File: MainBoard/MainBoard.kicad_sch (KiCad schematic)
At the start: 33 parts, among them J1 1761681-3, J2 Non-Inverting Input, J3 Inverting Input, J4 Output, J5 InvertedOutput, J6 Inverting Input, J7 Non-Inverting Input, J8 Output, J9 InvertedOutput, Q16 BC557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

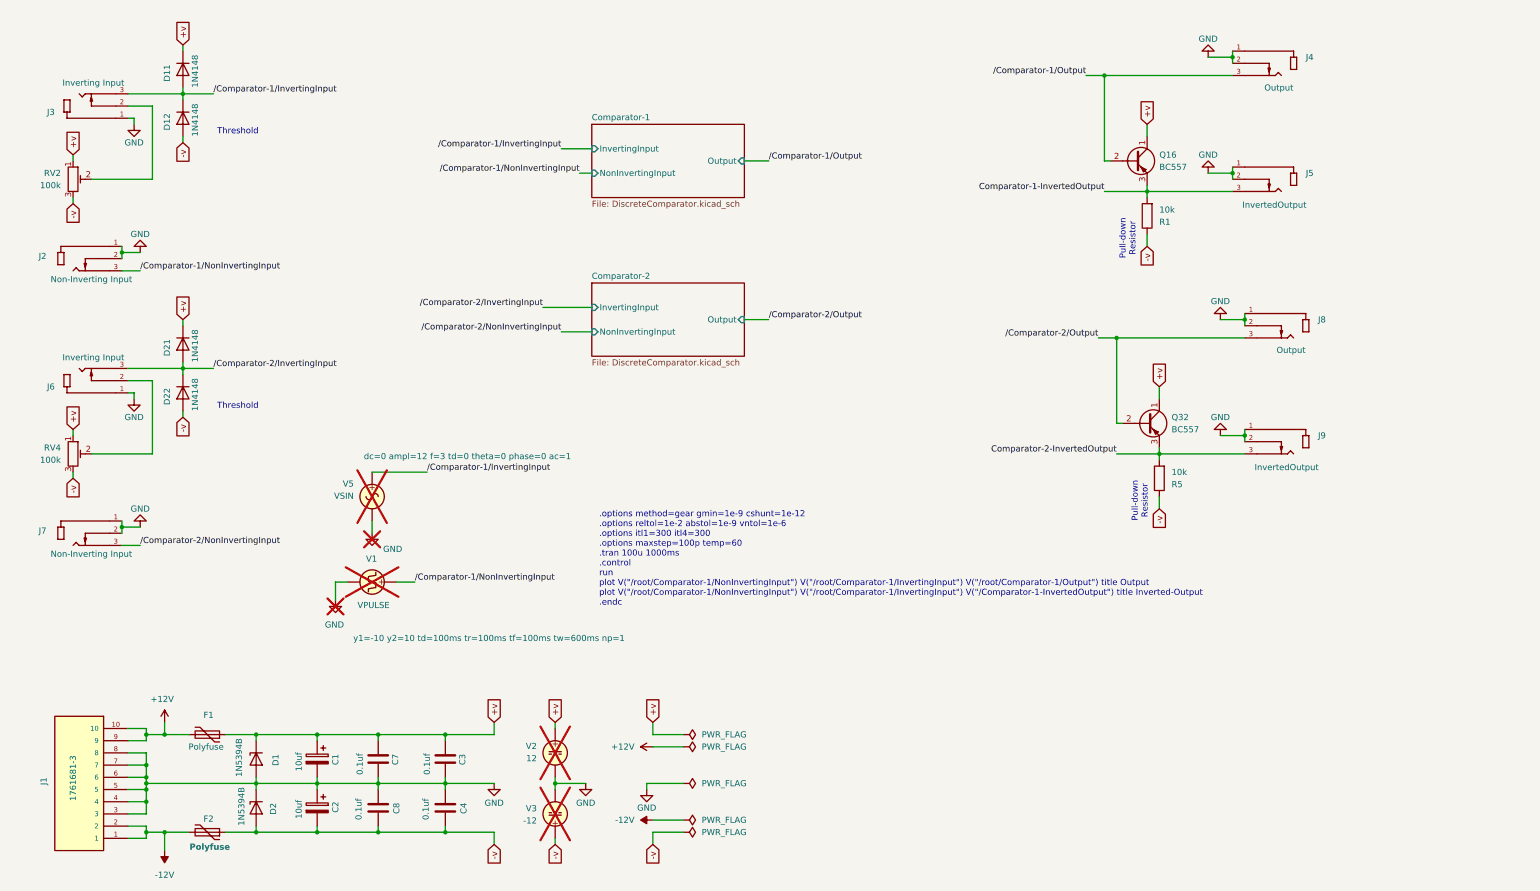
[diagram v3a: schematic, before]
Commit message: updated to be a dual comparator and/or window comparator
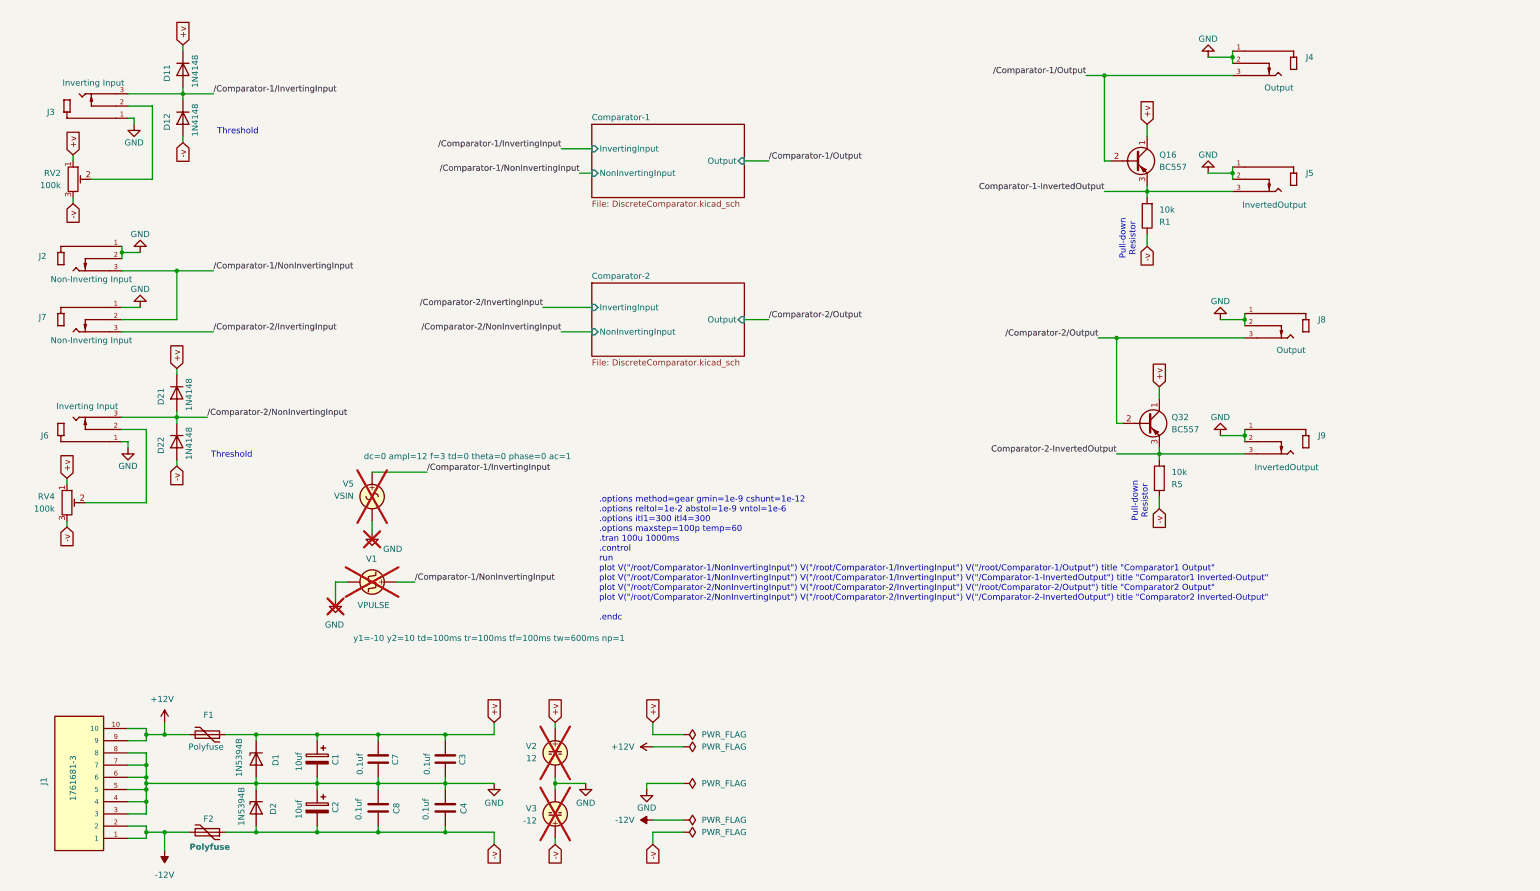
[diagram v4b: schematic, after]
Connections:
- net GND: no longer J7.2
- net /Comparator-1/NonInvertingInput: now also J7.2
- net /Comparator-2/InvertingInput: now also J7.3; no longer D21.2 (A), D22.1 (K), J6.3
- net /Comparator-2/NonInvertingInput: now also D21.2 (A), D22.1 (K), J6.3; no longer J7.3
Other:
- note added: ".options method=gear gmin=1e-9 cshunt=1e-12 .options reltol=1e-2 abstol=1e-9 vntol=1e-6 .options itl1=300 itl4=300 .options maxstep=100p temp=60 .tran 100u 1000ms .control run plot V("/root/Comparator-1/NonInvertingInput") V("/root/Comparator-1/InvertingInput") V("/root/Comparator-1/Output") title "Comparator1 Output" plot V("/root/Comparator-1/NonInvertingInput") V("/root/Comparator-1/InvertingI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"
- note removed: ".options method=gear gmin=1e-9 cshunt=1e-12 .options reltol=1e-2 abstol=1e-9 vntol=1e-6 .options itl1=300 itl4=300 .options maxstep=100p temp=60 .tran 100u 1000ms .control run plot V("/root/Comparator-1/NonInvertingInput") V("/root/Comparator-1/InvertingInput") V("/root/Comparator-1/Output") title Output plot V("/root/Comparator-1/NonInvertingInput") V("/root/Comparator-1/InvertingInput") V("/Com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"
- moved on the sheet: D21, D22, J6, J7, RV4

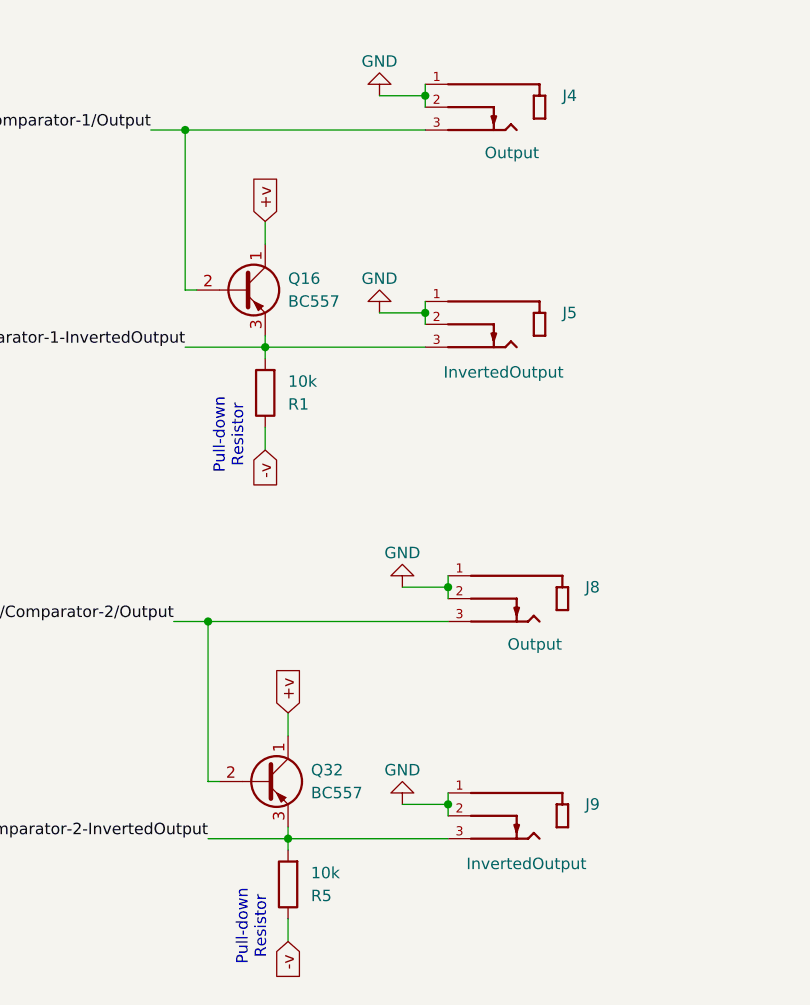
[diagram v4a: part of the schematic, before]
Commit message: fixed output connectors. probably should have ability in model to default them to open when running the simmulation (and keep the ring tied to ground. But , for now tying the ring to tip.
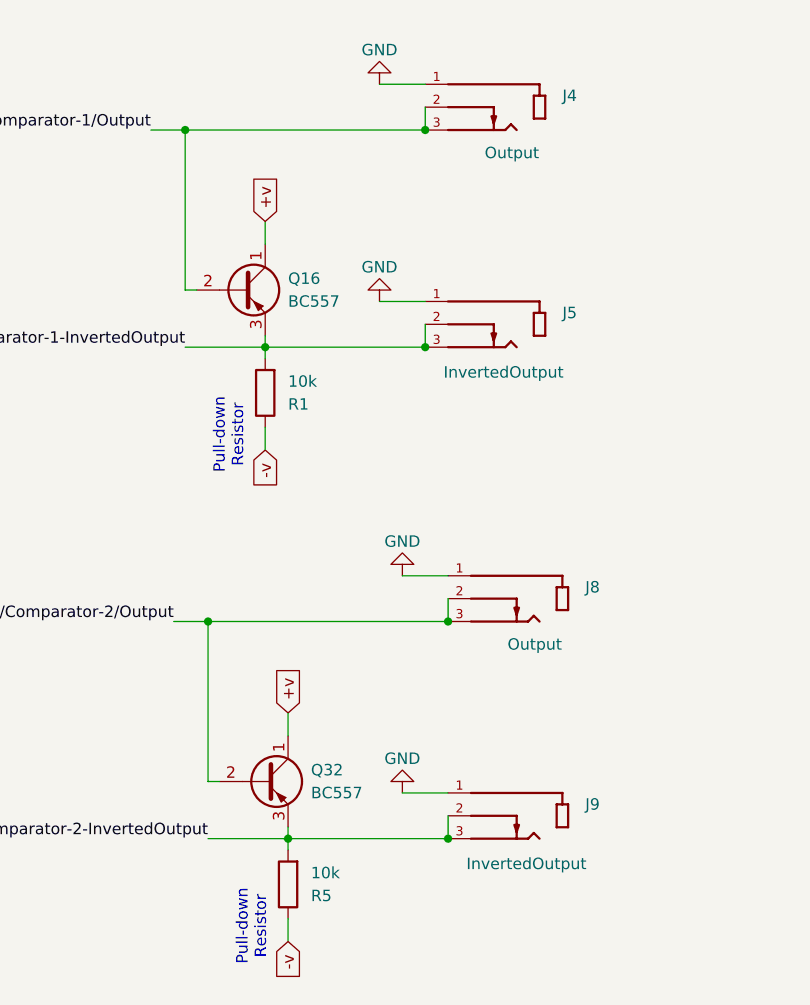
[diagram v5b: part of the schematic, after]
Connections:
- net Comparator-1-InvertedOutput: now also J5.2
- net Comparator-2-InvertedOutput: now also J9.2
- net GND: no longer J4.2, J5.2, J8.2, J9.2
- net /Comparator-1/Output: now also J4.2
- net /Comparator-2/Output: now also J8.2

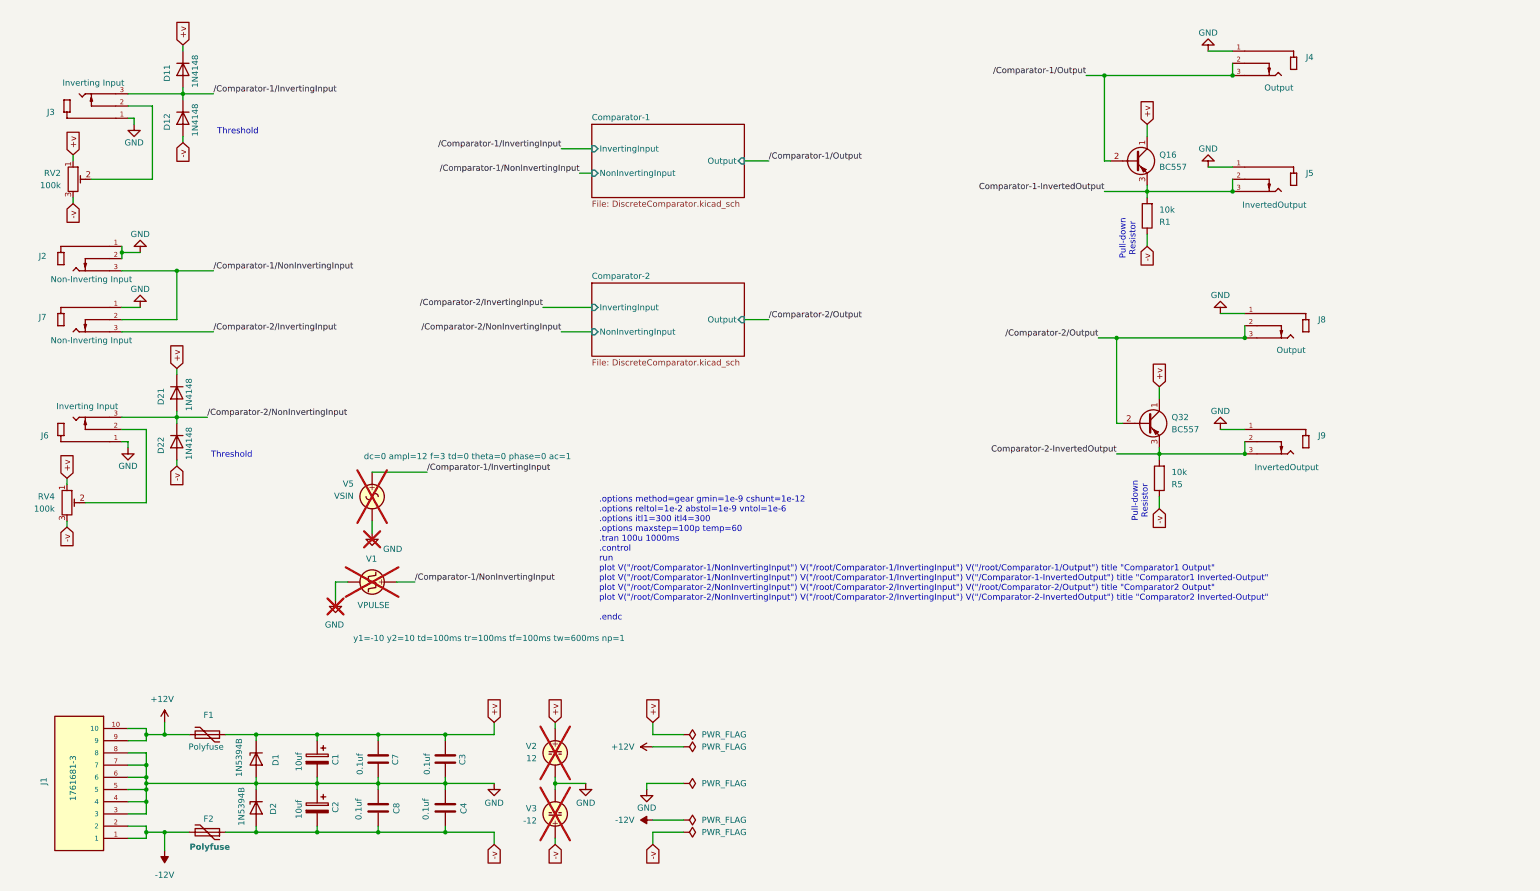
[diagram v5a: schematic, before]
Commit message: functional window comparator
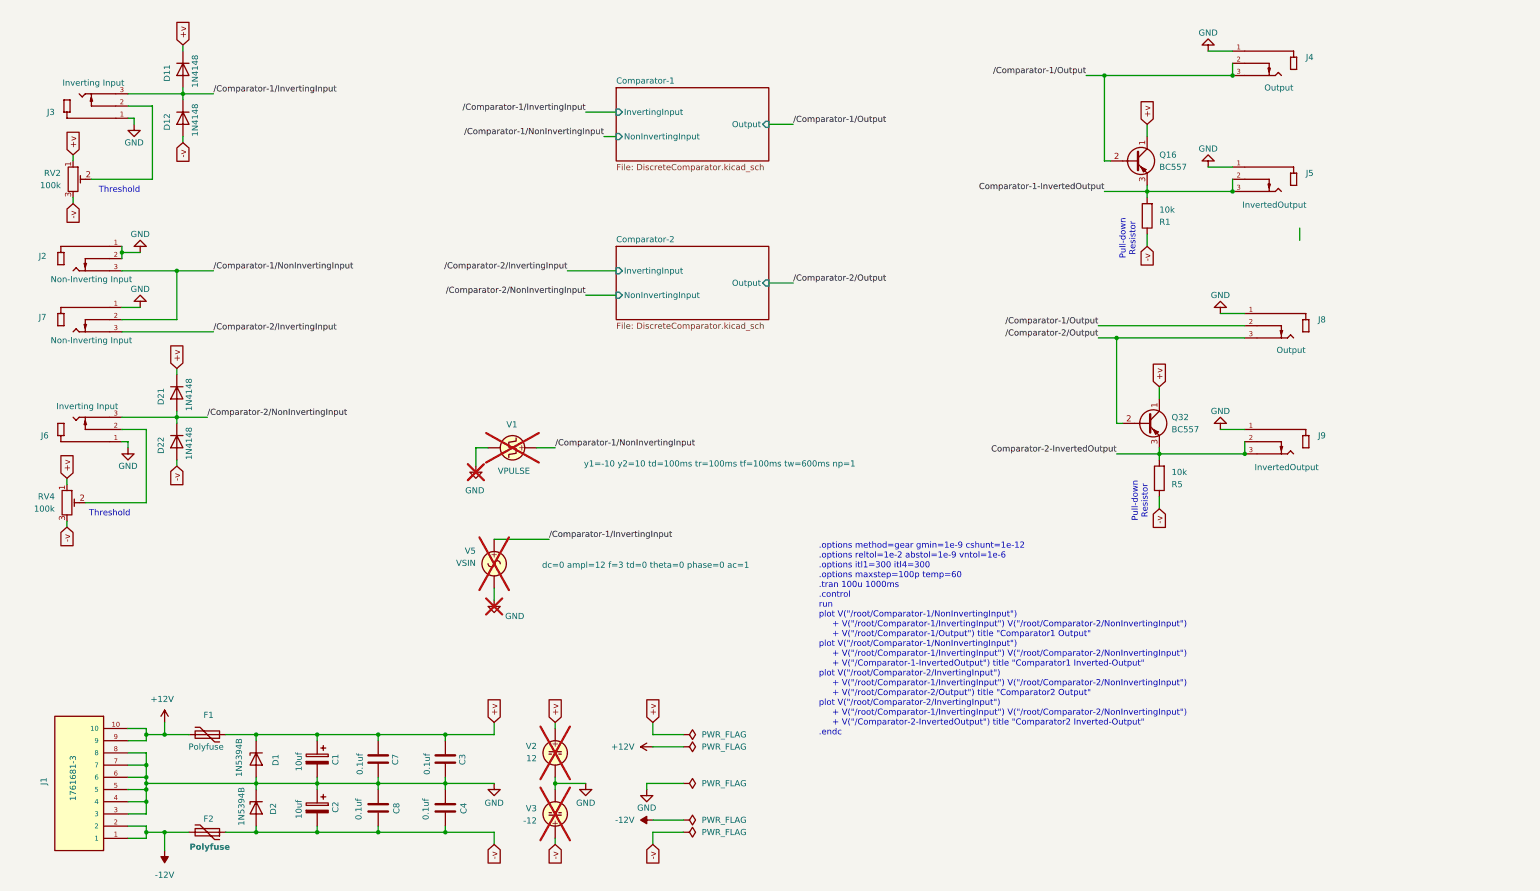
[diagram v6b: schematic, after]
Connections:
- net /Comparator-1/Output: now also J8.2
- net /Comparator-2/Output: no longer J8.2
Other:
- note added: ".options method=gear gmin=1e-9 cshunt=1e-12 .options reltol=1e-2 abstol=1e-9 vntol=1e-6 .options itl1=300 itl4=300 .options maxstep=100p temp=60 .tran 100u 1000ms .control run plot V("/root/Comparator-1/NonInvertingInput") + V("/root/Comparator-1/InvertingInput") V("/root/Comparator-2/NonInvertingInput") + V("/root/Comparator-1/Output") title "Comparator1 Output" plot V("/root/Comparator-1/NonInv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"
- note removed: ".options method=gear gmin=1e-9 cshunt=1e-12 .options reltol=1e-2 abstol=1e-9 vntol=1e-6 .options itl1=300 itl4=300 .options maxstep=100p temp=60 .tran 100u 1000ms .control run plot V("/root/Comparator-1/NonInvertingInput") V("/root/Comparator-1/InvertingInput") V("/root/Comparator-1/Output") title "Comparator1 Output" plot V("/root/Comparator-1/NonInvertingInput") V("/root/Comparator-1/InvertingI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"
- moved on the sheet: V1, V5

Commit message: added over-voltage protection on all inputs and outputs
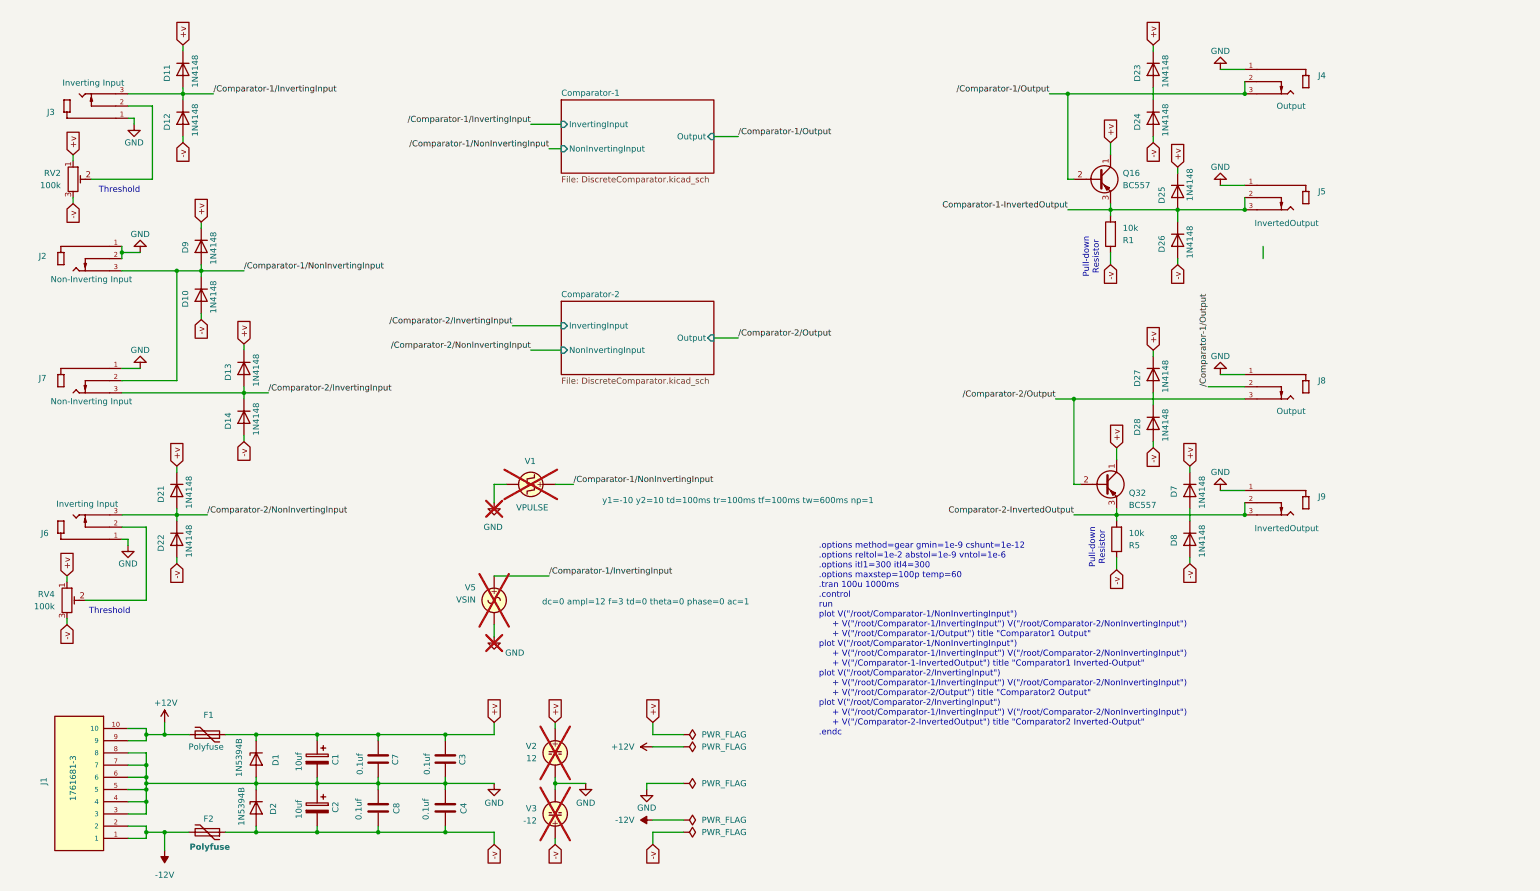
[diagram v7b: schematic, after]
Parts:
- added D10, D13, D14, D23, D24, D25, D26, D27, D28, D7, D8, D9: 1N4148, Diode_THT:D_DO-35_SOD27_P7.62mm_Horizontal, symbol Device:D
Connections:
- net +v: now also D13.1 (K), D23.1 (K), D25.1 (K), D27.1 (K), D7.1 (K), D9.1 (K)
- net -v: now also D10.2 (A), D14.2 (A), D24.2 (A), D26.2 (A), D28.2 (A), D8.2 (A)
- net Comparator-1-InvertedOutput: now also D25.2 (A), D26.1 (K)
- net /Comparator-1/NonInvertingInput: now also D10.1 (K), D9.2 (A)
- net /Comparator-2/InvertingInput: now also D13.2 (A), D14.1 (K)
- new net: D7.2 (A), D8.1 (K)
- new net: D27.2 (A), D28.1 (K)
- new net: D23.2 (A), D24.1 (K)
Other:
- moved on the sheet: D21, D22, J4, J5, J6, J7, J8, J9, Q16, Q32, R1, R5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
